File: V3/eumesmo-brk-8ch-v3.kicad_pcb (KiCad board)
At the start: 2 copper layers, 105 x 67.8 mm, 17 parts, among them J1 Jack RJ45, J10 250-206, J11 250-206, J12 250-206, J13 250-206, J2 Jack RJ45, J3 Jack RJ45, J4 Jack RJ45, J5 Jack RJ45, J6 Jack RJ45, J7 Jack RJ45, J8 Jack RJ45, J9 250-202

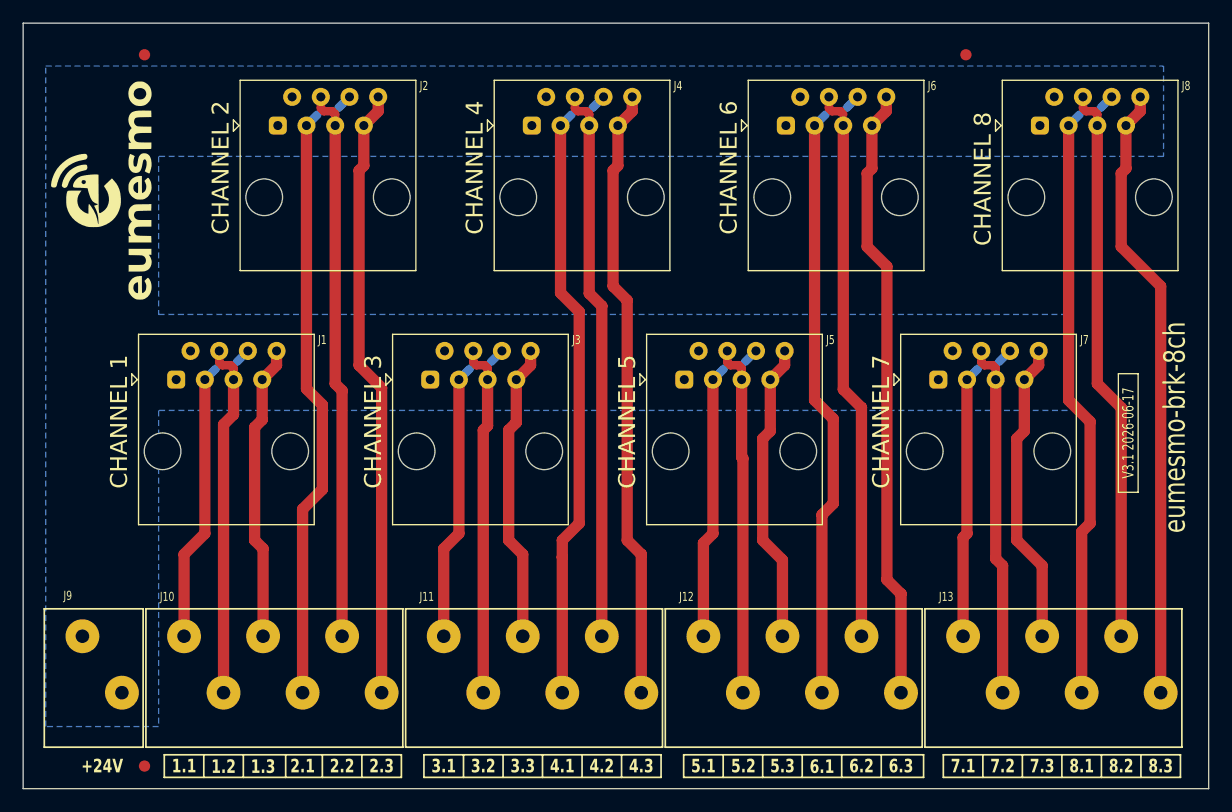
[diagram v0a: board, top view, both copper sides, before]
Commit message: Adjust board width to 103mm
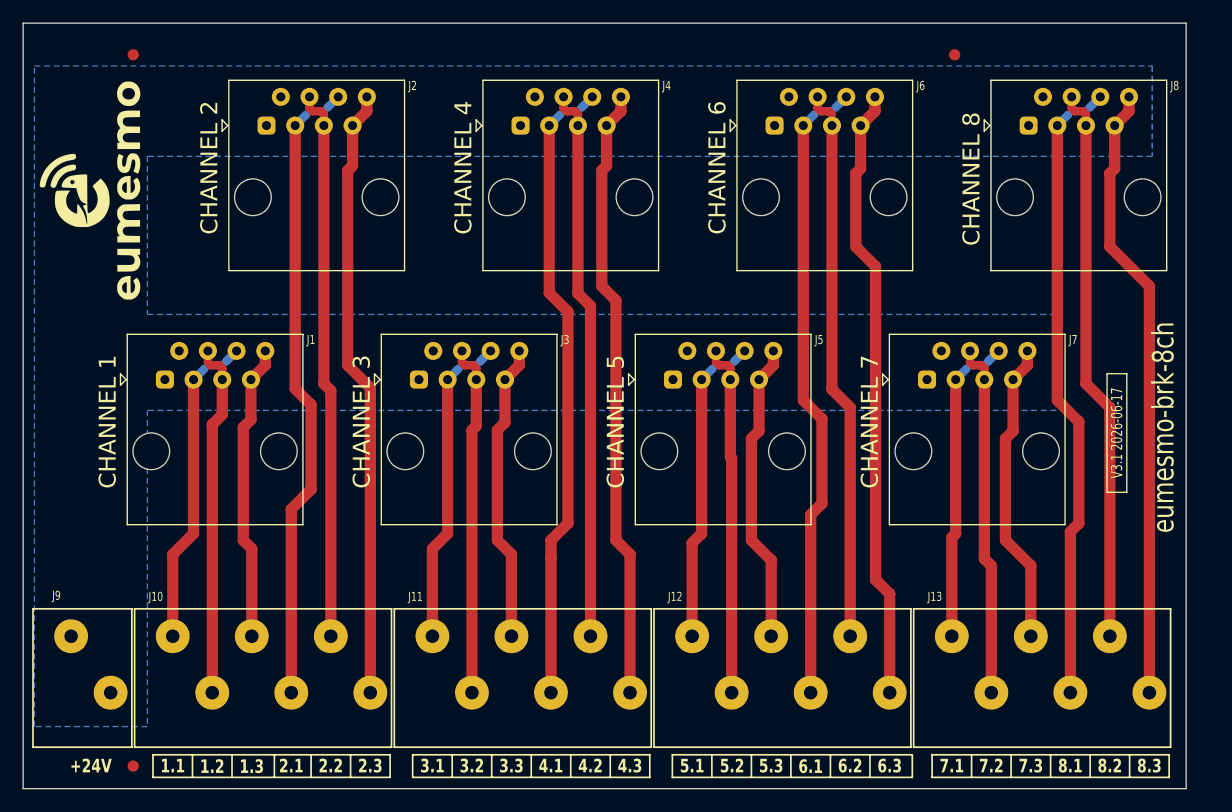
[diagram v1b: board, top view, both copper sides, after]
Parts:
- moved FID1 1.00 mm to (109.8, 65.0)
- moved FID2 1.00 mm to (109.8, 128.0)
- moved FID3 1.00 mm to (182.5, 65.0)
- moved G*** 1.00 mm to (106.0, 77.0)
- moved J1 1.00 mm to (117.0, 92.5)
- moved J10 1.00 mm to (122.0, 119.0)
- moved J11 1.00 mm to (145.0, 119.0)
- moved J12 1.00 mm to (168.0, 119.0)
- moved J13 1.00 mm to (191.0, 119.0)
- moved J2 1.00 mm to (126.0, 70.0)
- moved J3 1.00 mm to (139.5, 92.5)
- moved J4 1.00 mm to (148.5, 70.0)
- moved J5 1.00 mm to (162.0, 92.5)
- moved J6 1.00 mm to (171.0, 70.0)
- moved J7 1.00 mm to (184.5, 92.5)
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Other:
- board size 105 x 67.8 mm -> 103 x 67.8 mm
- board text added: "SUPORTES PCI METALTEX SP7 1x pé macho 9 mm 1x pé fêmea 9 mm 1x espaçador 45 mm 1x espaçador 30 mm 1x espaçador 10 mm Comprimento total 103 mm Largura da placa 67,8 mm"
- board text removed: "SUPORTES PCI METALTEX SP7 1x pé macho 9 mm 1x pé fêmea 9 mm 1x espaçador 45 mm 1x espaçador 30 mm Comprimento total 93 mm Largura da placa 67,8 mm"
